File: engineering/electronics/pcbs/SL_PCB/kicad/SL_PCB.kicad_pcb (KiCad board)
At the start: 2 copper layers, 200 x 115 mm, 1 part, among them J35 ET60S-D06-0-00-D06-X-V1-S

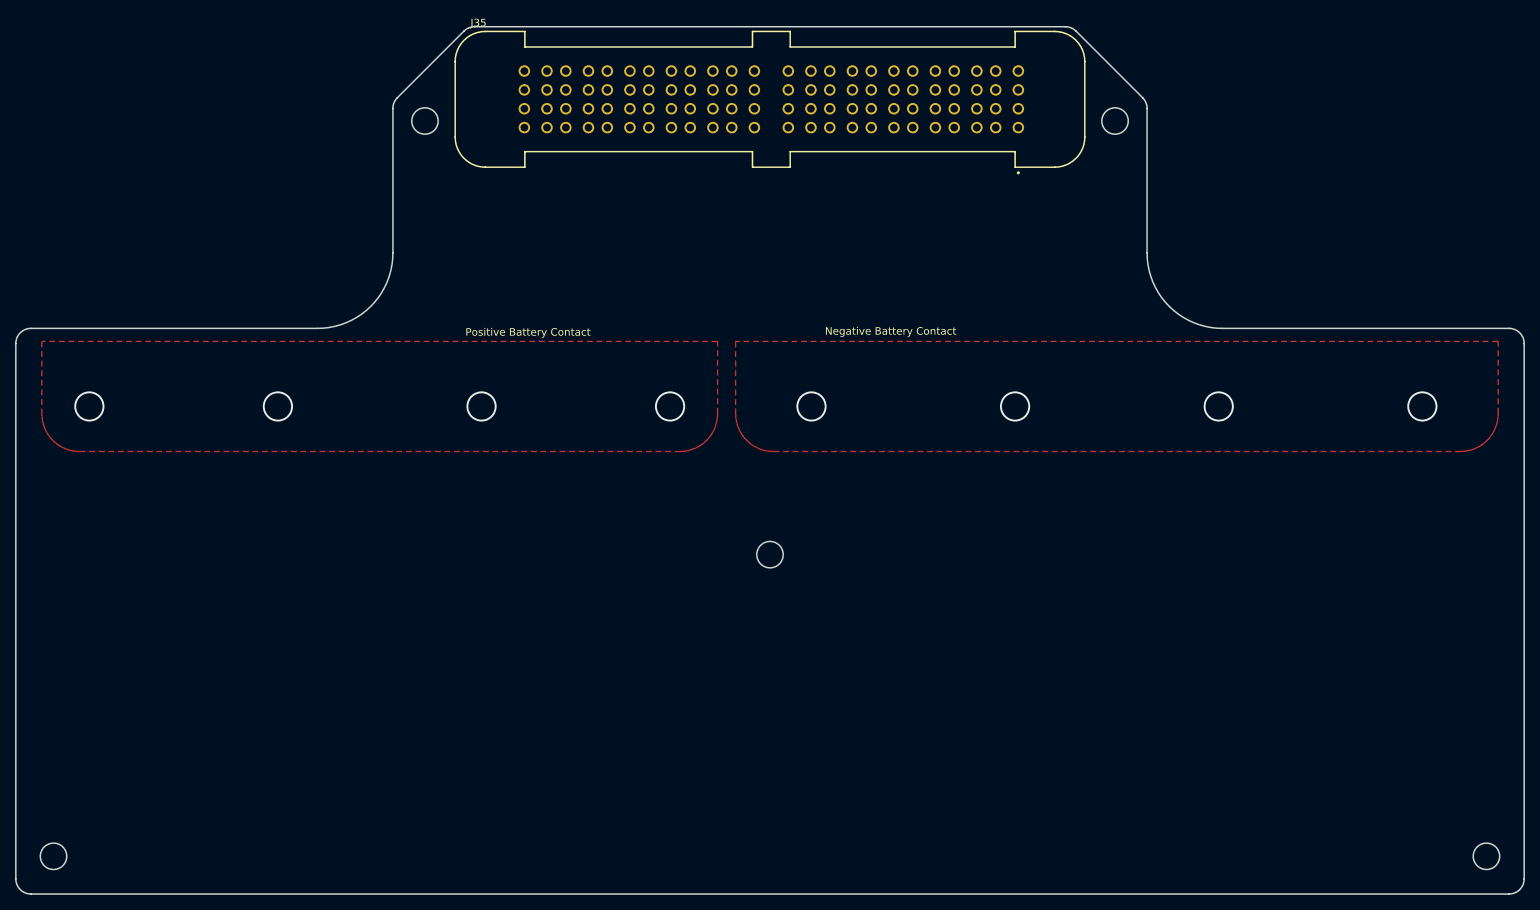
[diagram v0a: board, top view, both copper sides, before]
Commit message: feat: update sl_pcb kicad project from julius's latest project folder
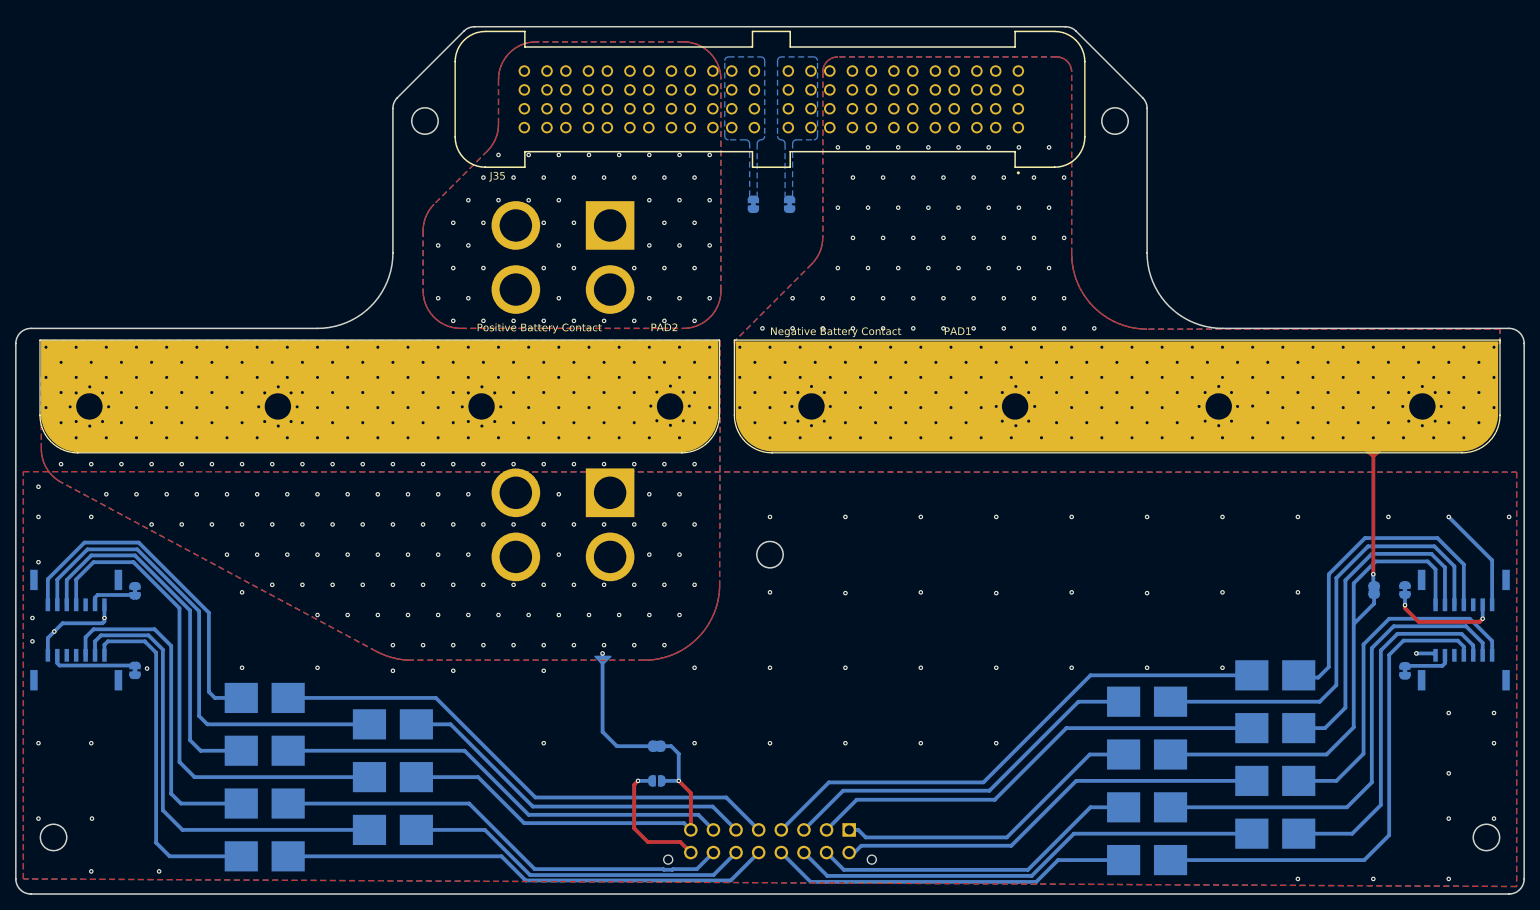
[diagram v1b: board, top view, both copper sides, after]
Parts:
- added CN1: ~, SL_PCB_EasyEDA_Lib:CONN-SMD_SM7B-GHS-TB-LF-SN, B.Cu at (292.0, 183.0)
- added CN2: ~, SL_PCB_EasyEDA_Lib:CONN-SMD_SM7B-GHS-TB-LF-SN, B.Cu at (292.0, 193.0)
- added CN3: ~, SL_PCB_EasyEDA_Lib:CONN-SMD_SM7B-GHS-TB-LF-SN, B.Cu at (108.0, 193.0)
- added CN4: ~, SL_PCB_EasyEDA_Lib:CONN-SMD_SM7B-GHS-TB-LF-SN, B.Cu at (108.0, 183.0)
- added CN5: ~, SL_PCB_EasyEDA_Lib:CONN-TH_430451612, B.Cu at (200.0, 216.0)
- added F0: ~, SL_PCB_EasyEDA_Lib:FUSE-SMD_L9.8-W5.1, B.Cu at (250.0, 204.5)
- added F1: ~, SL_PCB_EasyEDA_Lib:FUSE-SMD_L9.8-W5.1, B.Cu at (267.0, 208.0)
- added F10: ~, SL_PCB_EasyEDA_Lib:FUSE-SMD_L9.8-W5.1, B.Cu at (150.0, 200.5)
- added F11: ~, SL_PCB_EasyEDA_Lib:FUSE-SMD_L9.8-W5.1, B.Cu at (150.0, 214.5)
- added F12: ~, SL_PCB_EasyEDA_Lib:FUSE-SMD_L9.8-W5.1, B.Cu at (133.0, 204.0)
- added F13: ~, SL_PCB_EasyEDA_Lib:FUSE-SMD_L9.8-W5.1, B.Cu at (133.0, 211.0)
- added F14: ~, SL_PCB_EasyEDA_Lib:FUSE-SMD_L9.8-W5.1, B.Cu at (150.0, 207.5)
- added F2: ~, SL_PCB_EasyEDA_Lib:FUSE-SMD_L9.8-W5.1, B.Cu at (267.0, 201.0)
- added F3: ~, SL_PCB_EasyEDA_Lib:FUSE-SMD_L9.8-W5.1, B.Cu at (250.0, 211.5)
- added F4: ~, SL_PCB_EasyEDA_Lib:FUSE-SMD_L9.8-W5.1, B.Cu at (250.0, 197.5)
- added F5: ~, SL_PCB_EasyEDA_Lib:FUSE-SMD_L9.8-W5.1, B.Cu at (267.0, 215.0)
- added F6: ~, SL_PCB_EasyEDA_Lib:FUSE-SMD_L9.8-W5.1, B.Cu at (267.0, 194.0)
- added F7: ~, SL_PCB_EasyEDA_Lib:FUSE-SMD_L9.8-W5.1, B.Cu at (250.0, 218.5)
- added F8: ~, SL_PCB_EasyEDA_Lib:FUSE-SMD_L9.8-W5.1, B.Cu at (133.0, 197.0)
- added F9: ~, SL_PCB_EasyEDA_Lib:FUSE-SMD_L9.8-W5.1, B.Cu at (133.0, 218.0)
- added J1: AMT0450003DB0000G, SL_PCB:AMT0450003DB0000G, B.Cu at (178.8, 169.8)
- added J2: AMT0450003DB0000G, SL_PCB:AMT0450003DB0000G, B.Cu at (178.8, 134.3)
- added JP1: Jumper_2_Small_Bridged, SL_PCB:SL_SolderJumper-2_P1.3mm_Bridged_RoundedPad1.0x1.5mm, B.Cu at (280.1, 182.7)
- added JP2: Jumper_2_Small_Bridged, SL_PCB:SL_SolderJumper-2_P1.3mm_Bridged_RoundedPad1.0x1.5mm, B.Cu at (185.0, 203.4)
- added JP3: SolderJumper_2_Open, Jumper:SolderJumper-2_P1.3mm_Open_RoundedPad1.0x1.5mm, B.Cu at (185.0, 208.0)
- added JP4: SolderJumper_2_Bridged, Jumper:SolderJumper-2_P1.3mm_Bridged_RoundedPad1.0x1.5mm, B.Cu at (284.2, 182.7)
- added JP5: SolderJumper_2_Bridged, Jumper:SolderJumper-2_P1.3mm_Bridged_RoundedPad1.0x1.5mm, B.Cu at (284.2, 193.4)
- added JP6: SolderJumper_2_Bridged, Jumper:SolderJumper-2_P1.3mm_Bridged_RoundedPad1.0x1.5mm, B.Cu at (115.8, 193.3)
- added JP7: SolderJumper_2_Bridged, Jumper:SolderJumper-2_P1.3mm_Bridged_RoundedPad1.0x1.5mm, B.Cu at (115.8, 182.8)
- added JP8: SolderJumper_2_Bridged, Jumper:SolderJumper-2_P1.3mm_Bridged_RoundedPad1.0x1.5mm, B.Cu at (197.8, 131.6)
- added JP9: SolderJumper_2_Bridged, Jumper:SolderJumper-2_P1.3mm_Bridged_RoundedPad1.0x1.5mm, B.Cu at (202.6, 131.6)
- added PAD1: Negative_Terminal, SL_PCB:Longshot_Negative_Terminal, F.Cu at (200.0, 223.0)
- added PAD2: Positive_Terminal, SL_PCB:Longshot_Positive_Terminal, F.Cu at (200.0, 223.0)
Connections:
- net /BATT+ renamed /BATT+_Fused
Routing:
- net /VS_C6: track 0.00 -> 70.9 mm
- net /VS_C8: track 0.00 -> 69.6 mm
- net Net-(JP1-A): track 0.00 -> 67.0 mm
- net Net-(CN4-Pad4): track 0.00 -> 66.8 mm
- net Net-(CN2-Pad4): track 0.00 -> 66.4 mm
- net /VS_C9: track 0.00 -> 65.2 mm
- net Net-(CN2-Pad2): track 0.00 -> 64.3 mm
- net Net-(CN4-Pad2): track 0.00 -> 63.2 mm
- net /VS_C5: track 0.00 -> 63.0 mm
- net /VS_C2: track 0.00 -> 62.0 mm
- net Net-(CN3-Pad2): track 0.00 -> 61.8 mm
- net /VS_C13: track 0.00 -> 61.0 mm
- net /VS_C12: track 0.00 -> 60.7 mm
- net Net-(CN1-Pad3): track 0.00 -> 60.7 mm
- net /VS_C1: track 0.00 -> 57.3 mm
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- added copper zone on B.Cu, net /BATT+
- added copper zone on F.Cu, net /BATT+
- added copper zone on In1.Cu, net /BATT+
- added copper zone on In2.Cu, net /BATT+
- added copper zone on In3.Cu, net /BATT+
- added copper zone on In4.Cu, net /BATT+
- added copper zone on B.Cu, net /BATT+_Fused
- added copper zone on In1.Cu, net /BATT+_Fused
- added copper zone on In2.Cu, net /BATT+_Fused
- added copper zone on In3.Cu, net /BATT+_Fused
- added copper zone on In4.Cu, net /BATT+_Fused
- added copper zone on B.Cu, net /BATT-
- added copper zone on In1.Cu, net /BATT-
- added copper zone on In2.Cu, net /BATT-
- added copper zone on In3.Cu, net /BATT-
- added copper zone on In4.Cu, net /BATT-
- added copper zone on B.Cu, net /BCAN_H
- added copper zone on B.Cu, net /BCAN_L
- added copper zone on B.Cu, net GND
- added copper zone on F.Cu, net GND
- added copper zone on In1.Cu, net GND
- added copper zone on In2.Cu, net GND
- added copper zone on In3.Cu, net GND
- added copper zone on In4.Cu, net GND
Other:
- outline, holes or cut-outs redrawn
- copper layers 2 -> 6
- board text added: "ARROW"
- board text added: "CANH"
- board text added: "CANL"
- board text added: "Project Longshot"
- board text added: "SL_PCB_V1 (07/26)"
- board text removed: "Negative Battery Contact"
- board text removed: "Positive Battery Contact"
